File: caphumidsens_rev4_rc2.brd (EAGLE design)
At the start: 110 x 9 mm, 9 parts, among them IC1 555

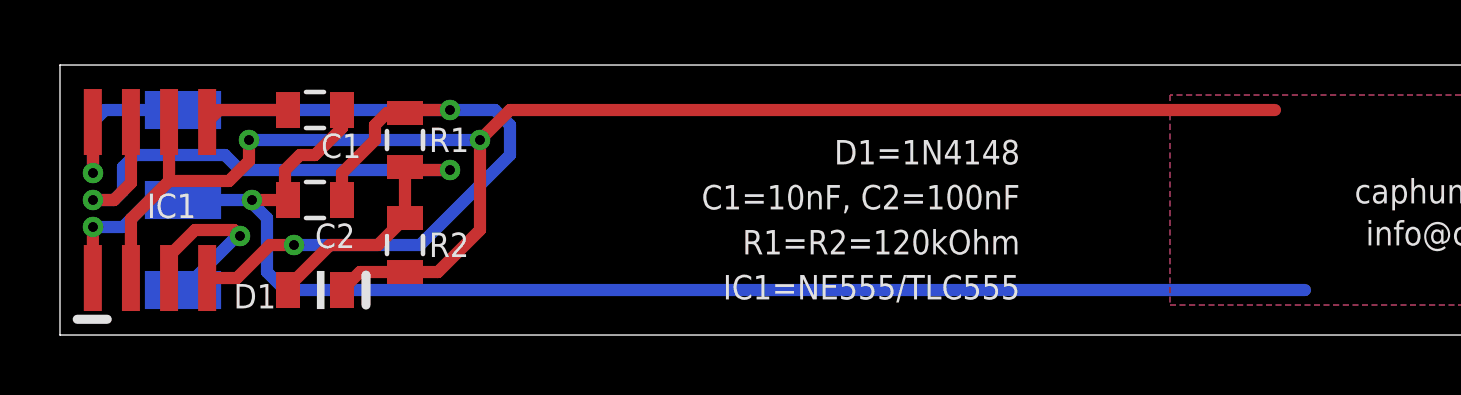
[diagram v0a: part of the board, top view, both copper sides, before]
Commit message: moved vias closer to their signal's pad's
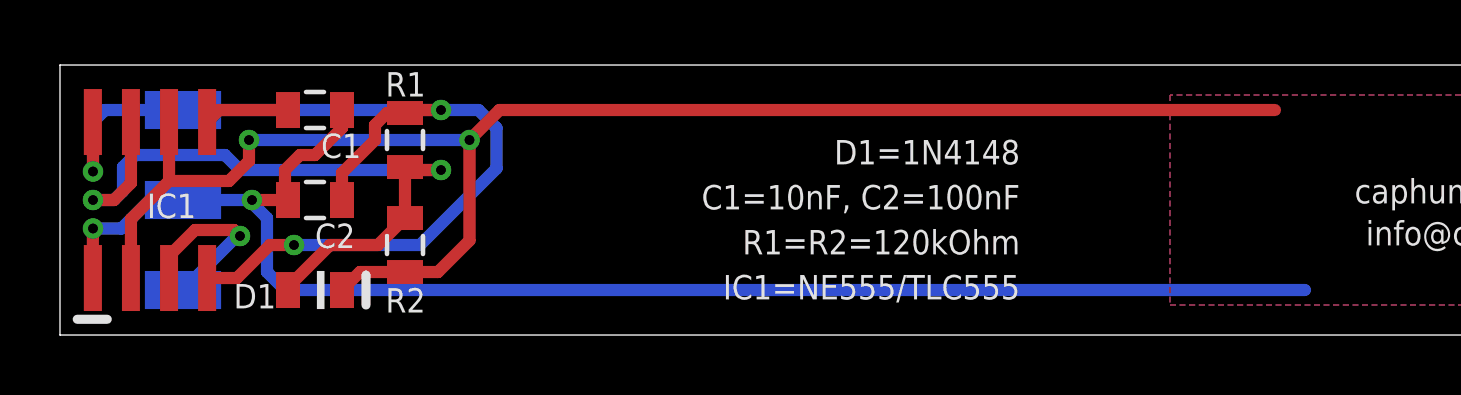
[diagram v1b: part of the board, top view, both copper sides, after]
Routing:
- net VCC: track 36.2 -> 35.1 mm
- net N$1: track 24.9 -> 24.3 mm
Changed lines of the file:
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@@
 <setting verticaltext="up"/>
 </settings>
-<grid distance="0.5" unitdist="mm" unit="mm" style="lines" multiple="1" display="yes" altdistance="0.1" altunitdist="mm" altunit="mm"/>
+<grid distance="0.05" unitdist="mm" unit="mm" style="lines" multiple="1" display="yes" altdistance="0.1" altunitdist="mm" altunit="mm"/>
 <layers>
 <layer number="1" name="Top" color="12" fill="1" visible="yes" active="yes"/>
@@
 <layer number="14" name="Route14" color="1" fill="6" visible="no" active="no"/>
 <layer number="15" name="Route15" color="4" fill="6" visible="no" active="no"/>
-<layer number="16" name="Bottom" color="9" fill="1" visible="no" active="yes"/>
+<layer number="16" name="Bottom" color="9" fill="1" visible="yes" active="yes"/>
 <layer number="17" name="Pads" color="2" fill="1" visible="yes" active="yes"/>
 <layer number="18" name="Vias" color="2" fill="1" visible="yes" active="yes"/>
 <layer number="19" name="Unrouted" color="6" fill="1" visible="yes" active="yes"/>
 <layer number="20" name="Dimension" color="15" fill="1" visible="yes" active="yes"/>
-<layer number="21" name="tPlace" color="7" fill="1" visible="no" active="yes"/>
-<layer number="22" name="bPlace" color="7" fill="1" visible="no" active="yes"/>
+<layer number="21" name="tPlace" color="7" fill="1" visible="yes" active="yes"/>
+<layer number="22" name="bPlace" color="7" fill="1" visible="yes" active="yes"/>
 <layer number="23" name="tOrigins" color="15" fill="1" visible="no" active="yes"/>
 <layer number="24" name="bOrigins" color="15" fill="1" visible="no" active="yes"/>
@@
 <layer number="28" name="bValues" color="7" fill="1" visible="no" active="yes"/>
 <layer number="29" name="tStop" color="7" fill="3" visible="yes" active="yes"/>
-<layer number="30" name="bStop" color="7" fill="6" visible="no" active="yes"/>
+<layer number="30" name="bStop" color="7" fill="6" visible="yes" active="yes"/>
 <layer number="31" name="tCream" color="7" fill="4" visible="no" active="yes"/>
 <layer number="32" name="bCream" color="7" fill="5" visible="no" active="yes"/>
@@
 <text x="8.7" y="5.9" size="0.8128" layer="25" font="vector" ratio="20">C1</text>
 <text x="8.5" y="2.9" size="0.8128" layer="25" font="vector" ratio="20">C2</text>
-<text x="12.3" y="6.1" size="0.8128" layer="25" font="vector" ratio="20">R1</text>
-<text x="12.3" y="2.6" size="0.8128" layer="25" font="vector" ratio="20">R2</text>
+<text x="10.85" y="7.95" size="0.8128" layer="25" font="vector" ratio="20">R1</text>
+<text x="10.85" y="0.75" size="0.8128" layer="25" font="vector" ratio="20">R2</text>
 <text x="7.2" y="1.7" size="0.8128" layer="25" font="vector" ratio="20" rot="R180">D1</text>
 <text x="2.9" y="3.9" size="0.8128" layer="25" font="vector" ratio="20">IC1</text>
@@
 <wire x1="10.6" y1="3" x2="11.5" y2="3.9" width="0.4064" layer="1"/>
 <via x="1.1" y="4.5" extent="1-16" drill="0.3302"/>
-<via x="13" y="5.5" extent="1-16" drill="0.3302"/>
-<wire x1="13" y1="5.5" x2="11.6" y2="5.5" width="0.4064" layer="1"/>
+<via x="12.7" y="5.5" extent="1-16" drill="0.3302"/>
+<wire x1="12.7" y1="5.5" x2="11.6" y2="5.5" width="0.4064" layer="1"/>
 <wire x1="11.6" y1="5.5" x2="11.5" y2="5.6" width="0.4064" layer="1"/>
 <wire x1="2.365" y1="7.1" x2="2.365" y2="5.065" width="0.4064" layer="1"/>
 <wire x1="9" y1="3" x2="7.6" y2="1.6" width="0.4064" layer="1"/>
 <wire x1="7.6" y1="1.6" x2="7.6" y2="1.5" width="0.4064" layer="1"/>
-<wire x1="13" y1="5.5" x2="6" y2="5.5" width="0.4064" layer="16"/>
+<wire x1="12.7" y1="5.5" x2="6" y2="5.5" width="0.4064" layer="16"/>
 <wire x1="2.1" y1="4.8" x2="2.1" y2="5.6" width="0.4064" layer="16"/>
 <wire x1="2.1" y1="5.6" x2="2.5" y2="6" width="0.4064" layer="16"/>
@@
 <wire x1="9.4" y1="5.4" x2="9.4" y2="4.5" width="0.4064" layer="1"/>
 <wire x1="9.4" y1="4.5" x2="9.4" y2="4.4" width="0.4064" layer="1"/>
-<via x="1.1" y="5.4" extent="1-16" drill="0.3302"/>
-<via x="13" y="7.5" extent="1-16" drill="0.3302"/>
-<wire x1="13" y1="7.5" x2="11.6" y2="7.5" width="0.4064" layer="1"/>
+<via x="1.1" y="5.45" extent="1-16" drill="0.3302"/>
+<via x="12.7" y="7.5" extent="1-16" drill="0.3302"/>
+<wire x1="12.7" y1="7.5" x2="11.6" y2="7.5" width="0.4064" layer="1"/>
 <wire x1="11.6" y1="7.5" x2="11.5" y2="7.4" width="0.4064" layer="1"/>
 <wire x1="1.1" y1="7.1" x2="1.5" y2="7.5" width="0.4064" layer="16"/>
-<wire x1="13" y1="7.5" x2="14.5" y2="7.5" width="0.4064" layer="16"/>
-<wire x1="14.5" y1="7.5" x2="15" y2="7" width="0.4064" layer="16"/>
-<wire x1="15" y1="7" x2="15" y2="6" width="0.4064" layer="16"/>
-<wire x1="15" y1="6" x2="12" y2="3" width="0.4064" layer="16"/>
+<wire x1="12.7" y1="7.5" x2="13.95" y2="7.5" width="0.4064" layer="16"/>
+<wire x1="13.95" y1="7.5" x2="14.55" y2="6.9" width="0.4064" layer="16"/>
+<wire x1="14.55" y1="6.9" x2="14.55" y2="5.55" width="0.4064" layer="16"/>
+<wire x1="14.55" y1="5.55" x2="12" y2="3" width="0.4064" layer="16"/>
 <via x="7.8" y="3" extent="1-16" drill="0.3302"/>
 <wire x1="5.9" y1="1.9" x2="4.905" y2="1.9" width="0.4064" layer="1"/>
 <wire x1="1.095" y1="7.1" x2="1.1" y2="7.095" width="0.4064" layer="1"/>
-<wire x1="1.1" y1="7.095" x2="1.1" y2="5.4" width="0.4064" layer="1"/>
+<wire x1="1.1" y1="7.095" x2="1.1" y2="5.45" width="0.4064" layer="1"/>
 <wire x1="4.1" y1="7.5" x2="1.5" y2="7.5" width="0.4064" layer="16"/>
-<wire x1="1.1" y1="5.4" x2="1.1" y2="7.1" width="0.4064" layer="16"/>
-<wire x1="4.1" y1="7.5" x2="13" y2="7.5" width="0.4064" layer="16"/>
+<wire x1="1.1" y1="5.45" x2="1.1" y2="7.1" width="0.4064" layer="16"/>
+<wire x1="4.1" y1="7.5" x2="12.7" y2="7.5" width="0.4064" layer="16"/>
 <wire x1="7.8" y1="3" x2="12" y2="3" width="0.4064" layer="16"/>
 <wire x1="7.8" y1="3" x2="7" y2="3" width="0.4064" layer="1"/>
@@
 <wire x1="9.4" y1="6.9" x2="9.4" y2="7.5" width="0.4064" layer="1"/>
 <wire x1="7.5" y1="4.6" x2="7.4" y2="4.5" width="0.4064" layer="1"/>
-<via x="1.1" y="3.6" extent="1-16" drill="0.3302"/>
+<via x="1.1" y="3.55" extent="1-16" drill="0.3302"/>
 <via x="6.4" y="4.5" extent="1-16" drill="0.3302"/>
 <wire x1="7.5" y1="1.5" x2="41.5" y2="1.5" width="0.4064" layer="16"/>
-<wire x1="1.1" y1="3.6" x2="1.095" y2="3.695" width="0.4064" layer="1"/>
-<wire x1="1.095" y1="3.695" x2="1.095" y2="1.9" width="0.4064" layer="1"/>
-<wire x1="2.1" y1="3.6" x2="3" y2="4.5" width="0.4064" layer="16"/>
+<wire x1="1.1" y1="3.55" x2="1.095" y2="3.295" width="0.4064" layer="1"/>
+<wire x1="1.095" y1="3.295" x2="1.095" y2="1.9" width="0.4064" layer="1"/>
+<wire x1="2.05" y1="3.55" x2="3" y2="4.5" width="0.4064" layer="16"/>
 <wire x1="3" y1="4.5" x2="4.1" y2="4.5" width="0.4064" layer="16"/>
 <wire x1="4.1" y1="4.5" x2="6.4" y2="4.5" width="0.4064" layer="16"/>
@@
 <wire x1="6.9" y1="3.9" x2="6.4" y2="4.4" width="0.4064" layer="16"/>
 <wire x1="6.4" y1="4.4" x2="6.4" y2="4.5" width="0.4064" layer="16"/>
-<wire x1="2.1" y1="3.6" x2="1.1" y2="3.6" width="0.4064" layer="16"/>
+<wire x1="2.05" y1="3.55" x2="1.1" y2="3.55" width="0.4064" layer="16"/>
 </signal>
 <signal name="CAP+">
@@
 <via x="6.3" y="6.5" extent="1-16" drill="0.3302"/>
 <wire x1="12.6" y1="2.1" x2="11.5" y2="2.1" width="0.4064" layer="1"/>
-<wire x1="15" y1="7.5" x2="40.5" y2="7.5" width="0.4064" layer="1"/>
-<wire x1="12.6" y1="2.1" x2="14" y2="3.5" width="0.4064" layer="1"/>
-<wire x1="14" y1="3.5" x2="14" y2="6.5" width="0.4064" layer="1"/>
-<wire x1="14" y1="6.5" x2="15" y2="7.5" width="0.4064" layer="1"/>
-<via x="14" y="6.5" extent="1-16" drill="0.3302"/>
-<wire x1="6.3" y1="6.5" x2="14" y2="6.5" width="0.4064" layer="16"/>
+<wire x1="14.65" y1="7.5" x2="40.5" y2="7.5" width="0.4064" layer="1"/>
+<wire x1="12.6" y1="2.1" x2="13.65" y2="3.15" width="0.4064" layer="1"/>
+<wire x1="13.65" y1="3.15" x2="13.65" y2="6.5" width="0.4064" layer="1"/>
+<wire x1="13.65" y1="6.5" x2="14.65" y2="7.5" width="0.4064" layer="1"/>
+<via x="13.65" y="6.5" extent="1-16" drill="0.3302"/>
+<wire x1="6.3" y1="6.5" x2="13.65" y2="6.5" width="0.4064" layer="16"/>
 <wire x1="5.635" y1="5.135" x2="6.3" y2="5.8" width="0.4064" layer="1"/>
 <wire x1="6.3" y1="5.8" x2="6.3" y2="6.5" width="0.4064" layer="1"/>
